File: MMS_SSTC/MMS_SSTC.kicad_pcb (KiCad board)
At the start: 2 copper layers, 80 x 80 mm, 39 parts, among them J1 Screw_Terminal_01x02, J2 Screw_Terminal_01x02, Q1 FQA8N100C, U1 NE555P, U2 UCC37322P, U3 LM7812_TO220, U4 LM7805_TO220, Y1 CXO_DIP8

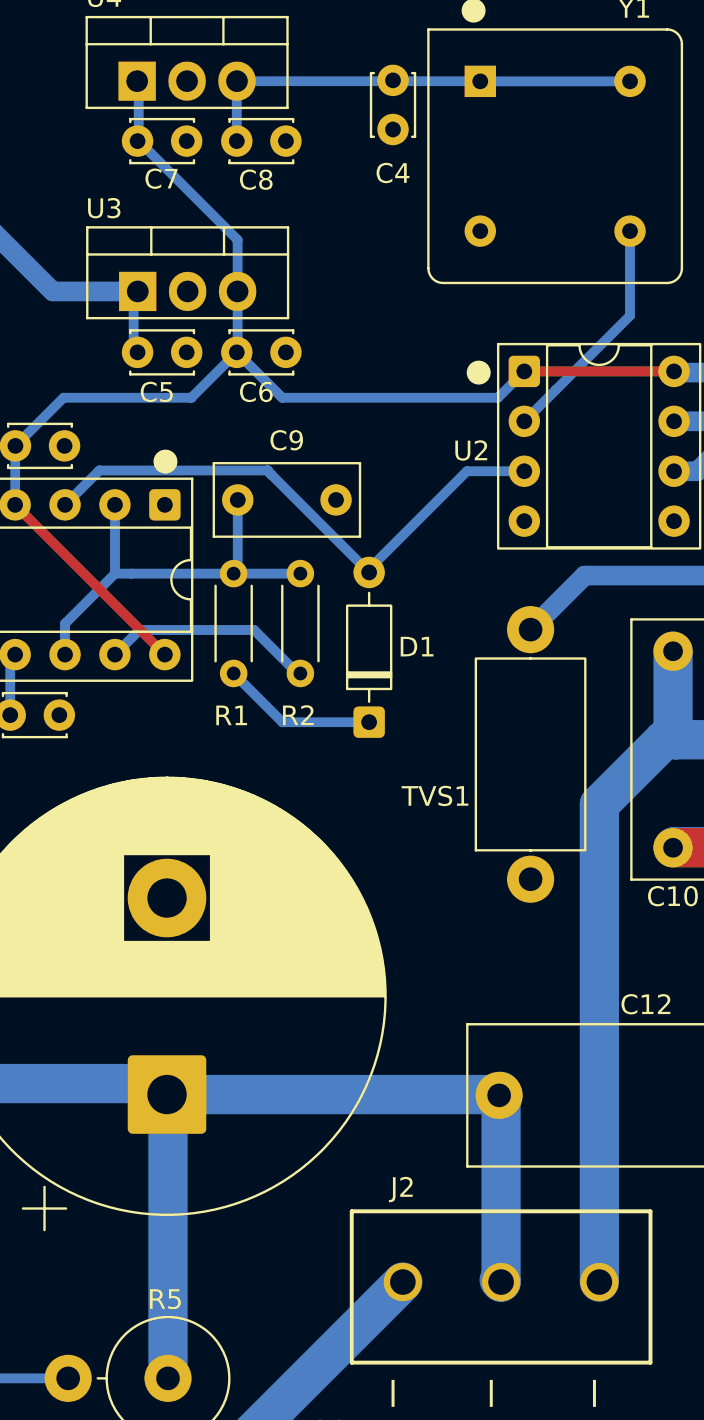
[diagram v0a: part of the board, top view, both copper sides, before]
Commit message: Clean up PCB after build test, add heat sink to assembly
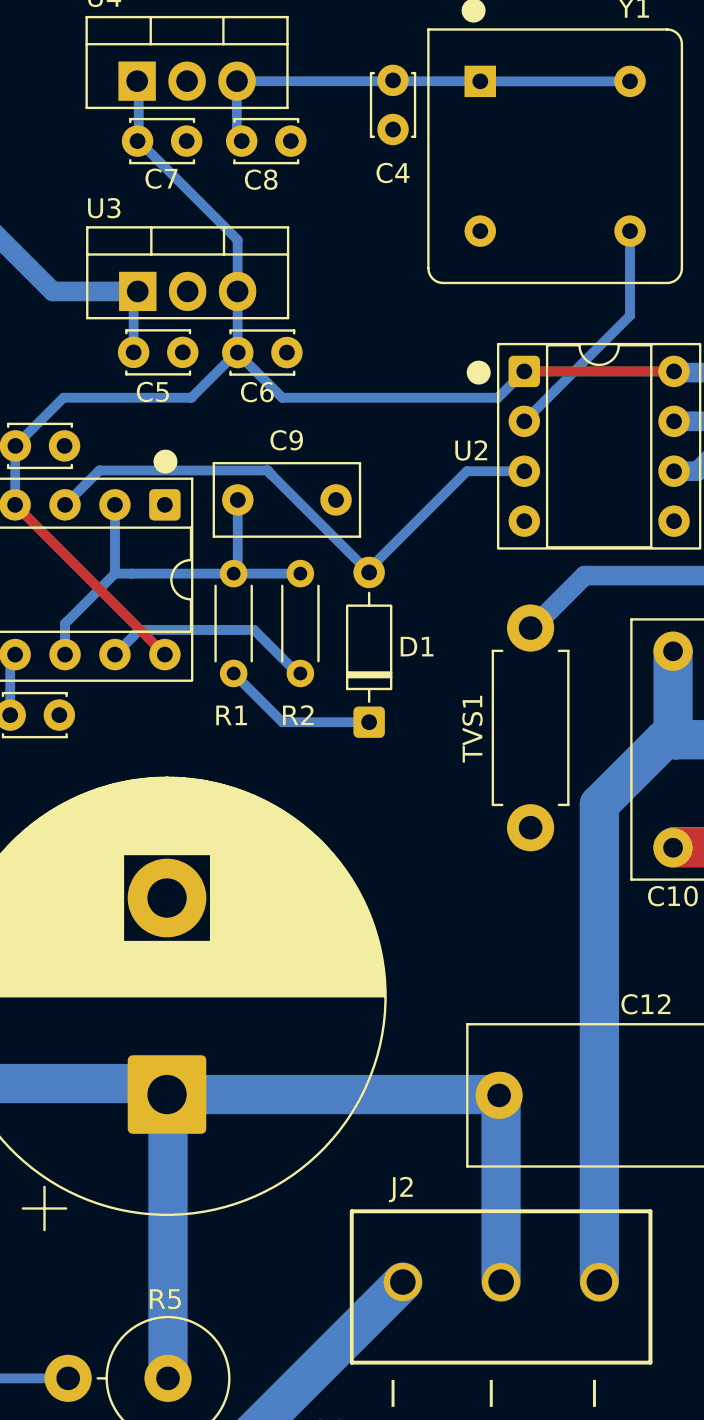
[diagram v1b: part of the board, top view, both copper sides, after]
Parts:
- TVS1: footprint Diode_THT:D_DO-27_P12.70mm_Horizontal -> Diode_THT:D_DO-15_P10.16mm_Horizontal
- moved TVS1 2.62 mm to (154.5, 109.5)
- moved C8 0.25 mm to (139.8, 74.5)
- moved C5 0.20 mm to (134.3, 85.3)
- moved C6 0.05 mm to (139.6, 85.3)
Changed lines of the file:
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@@
 	(footprint "Capacitor_THT:C_Disc_D3.0mm_W2.0mm_P2.50mm"
 		(layer "F.Cu")
-		(at 139.55 74.54)
+		(at 139.8 74.54)
 		(descr "C, Disc series, Radial, pin pitch=2.50mm, diameter*width=3*2mm^2, Capacitor")
 		(tags "C Disc series Radial pin pitch 2.50mm diameter 3mm width 2mm Capacitor")
@@
 	(footprint "Capacitor_THT:C_Disc_D3.0mm_W2.0mm_P2.50mm"
 		(layer "F.Cu")
-		(at 134.5 85.29)
+		(at 134.3 85.29)
 		(descr "C, Disc series, Radial, pin pitch=2.50mm, diameter*width=3*2mm^2, Capacitor")
 		(tags "C Disc series Radial pin pitch 2.50mm diameter 3mm width 2mm Capacitor")
@@
 	(footprint "Capacitor_THT:C_Disc_D3.0mm_W2.0mm_P2.50mm"
 		(layer "F.Cu")
-		(at 139.55 85.29)
+		(at 139.6 85.3)
 		(descr "C, Disc series, Radial, pin pitch=2.50mm, diameter*width=3*2mm^2, Capacitor")
 		(tags "C Disc series Radial pin pitch 2.50mm diameter 3mm width 2mm Capacitor")
@@
 		)
 	)
-	(footprint "Diode_THT:D_DO-27_P12.70mm_Horizontal"
+	(footprint "Diode_THT:D_DO-15_P10.16mm_Horizontal"
 		(layer "F.Cu")
-		(at 154.5 112.1 90)
-		(descr "Diode, DO-27 series, Axial, Horizontal, pin pitch=12.7mm, length*diameter=9.52*5.33mm^2, http://www.slottechforum.com/slotinfo/Techstuff/CD2%20Diodes%20and%20Transistors/Cases/Diode%20DO-27.jpg")
-		(tags "Diode DO-27 series Axial Horizontal pin pitch 12.7mm  length 9.52mm diameter 5.33mm")
+		(at 154.5 109.48 90)
+		(descr "Diode, DO-15 series, Axial, Horizontal, pin pitch=10.16mm, length*diameter=7.6*3.6mm^2, http://www.diodes.com/_files/packages/DO-15.pdf")
+		(tags "Diode DO-15 series Axial Horizontal pin pitch 10.16mm  length 7.6mm diameter 3.6mm")
 		(property "Reference" "TVS1"
-			(at 4.2 -4.8 180)
+			(at 5.08 -2.92 90)
 			(layer "F.SilkS")
 			(effects
@@
 		)
 		(property "Value" "16.7V"
-			(at 6.35 3.785 90)
+			(at 5.08 2.92 90)
 			(layer "F.Fab")
 			(effects
@@
 				(font
 					(size 1.27 1.27)
-					(thickness 0.15)
 				)
 			)
@@
 				(font
 					(size 1.27 1.27)
+				)
+			)
+		)
+		(property "KiLib_Generator" "diode/THT"
+			(at 0 0 90)
+			(layer "F.SilkS")
+			(hide yes)
+			(effects
+				(font
+					(size 1 1)
 					(thickness 0.15)
 				)
@@
 		(sheetname "/")
 		(sheetfile "MMS_SSTC.kicad_sch")
-		(units
-			(unit
-				(name "A")
-				(pins "1" "2")
-			)
-		)
 		(attr through_hole)
 		(duplicate_pad_numbers_are_jumpers no)
 		(fp_line
-			(start 11.26 0)
-			(end 11.23 0)
+			(start 9 -1.92)
+			(end 9 -1.44)
 			(stroke
 				(width 0.12)
@@
 		)
 		(fp_line
-			(start 1.44 0)
-			(end 1.47 0)
+			(start 1.16 -1.92)
+			(end 9 -1.92)
 			(stroke
 				(width 0.12)
@@
 			(layer "F.SilkS")
 		)
-		(fp_rect
-			(start 1.47 -2.785)
-			(end 11.23 2.785)
+		(fp_line
+			(start 1.16 -1.44)
+			(end 1.16 -1.92)
+			(stroke
+				(width 0.12)
+				(type solid)
+			)
+			(layer "F.SilkS")
+		)
+		(fp_line
+			(start 1.16 1.44)
+			(end 1.16 1.92)
+			(stroke
+				(width 0.12)
+				(type solid)
+			)
+			(layer "F.SilkS")
+		)
+		(fp_line
+			(start 9 1.92)
+			(end 9 1.44)
+			(stroke
+				(width 0.12)
+				(type solid)
+			)
+			(layer "F.SilkS")
+		)
+		(fp_line
+			(start 1.16 1.92)
+			(end 9 1.92)
 			(stroke
 				(width 0.12)
 				(type solid)
 			)
-			(fill no)
 			(layer "F.SilkS")
 		)
 		(fp_rect
-			(start -1.45 -2.92)
-			(end 14.15 2.92)
+			(start -1.45 -2.05)
+			(end 11.61 2.05)
 			(stroke
 				(width 0.05)
@@
 		)
 		(fp_line
-			(start 12.7 0)
-			(end 11.11 0)
+			(start 10.16 0)
+			(end 8.88 0)
 			(stroke
 				(width 0.1)
@@
 		(fp_line
 			(start 0 0)
-			(end 1.59 0)
+			(end 1.28 0)
 			(stroke
 				(width 0.1)
@@
 		)
 		(fp_rect
-			(start 1.59 -2.665)
-			(end 11.11 2.665)
+			(start 1.28 -1.8)
+			(end 8.88 1.8)
 			(stroke
 				(width 0.1)
@@
 		)
 		(fp_text user "${REFERENCE}"
-			(at 7.064 0 90)
+			(at 5.65 0 90)
 			(layer "F.Fab")
 			(effects
@@
 		)
 		(pad "2" thru_hole circle
-			(at 12.7 0 90)
+			(at 10.16 0 90)
 			(size 2.4 2.4)
 			(drill 1.2)
@@
 		)
 		(embedded_fonts no)
-		(model "${KICAD9_3DMODEL_DIR}/Diode_THT.3dshapes/D_DO-27_P12.70mm_Horizontal.step"
+		(model "${KICAD10_3DMODEL_DIR}/Diode_THT.3dshapes/D_DO-15_P10.16mm_Horizontal.step"
 			(offset
 				(xyz 0 0 0)
@@
 	)
 	(segment
-		(start 152.9 132.5)
-		(end 153 132.6)
-		(width 2)
-		(layer "B.Cu")
-		(net "+170V")
-	)
-	(segment
 		(start 162.99 91.34)
 		(end 165.3 89.03)
@@
 		)
 	)
-	(group ""
-		(members "175a56ea-8fee-4fcb-9bce-bff846cb96c2" "1ac42987-1cc8-4131-8ea1-be100f3d4653"
-			"2c3b3042-3c52-48dd-af57-090bd6d326e5" "34143c22-21ec-440c-b1ed-2d7513854fca"
-			"355b98f4-525d-4baf-8700-22003f3cc0c2" "453af49a-d00f-4df1-b29b-a2d490fdd1ea"
-			"5a939f4a-45fe-4a46-b9ed-41afbd8eb7b0" "5b99613d-31bd-469f-b295-5eaa014b474b"
-			"68af7112-564f-44fb-9545-030e8fee29d0" "692f0a5a-0a85-448a-ac65-f9188ba53d23"
-			"7fa44c74-5361-4881-b1aa-b23759aec6ca" "88a81a6e-68f8-4c7d-ba78-aafcea9e31e5"
-			"893a3ebd-0fd1-4787-a88d-403bf9eb3d79" "95c6dcbf-2410-44d3-9606-f02159baee44"
-			"9a3f79d6-8322-40c0-a863-76c2e8428029" "9c227b80-f46e-4466-8091-95c8972f8ddf"
-			"9f9d70aa-5f02-41cb-b8d5-829343708e1b" "ba4580cb-5e39-47a8-b134-fc27c1b810aa"
-			"c315f831-ca56-49ab-8ca2-71e26c01af54" "c8a25969-9fb0-4973-8110-14b8e3b67a6c"
-			"d672387f-5f49-44de-af3d-c9d97789ffad" "e435c55b-4fdd-465c-86f9-fd9303cf9e19"
-			"e7e4c3a0-6e6a-423f-a0e8-d109c311fde4" "f36cd85c-1a5d-495f-84b8-259e4f6d7740"
-		)
-	)
